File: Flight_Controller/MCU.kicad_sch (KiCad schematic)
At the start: 1 part, among them U1 STM32H743VITx

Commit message: Schem V1 Done!
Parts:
- added C16, C18, C19, C20, C21, C22, C23, C27: 100nF, PCM_JLCPCB:C_0603, symbol PCM_JLCPCB-Capacitors:0603,100nF
- added C17: 4.7uF, PCM_JLCPCB:C_0603, symbol PCM_JLCPCB-Capacitors:0603,4.7uF
- added C25, C26: 12pF, PCM_JLCPCB:C_0603, symbol PCM_JLCPCB-Capacitors:0603,12pF
- added C28, C29: 2.2uF, PCM_JLCPCB:C_0603, symbol PCM_JLCPCB-Capacitors:0603,2.2uF
- added J10: USB_C_Receptacle_USB2.0_16P, symbol Connector:USB_C_Receptacle_USB2.0_16P
- added J11: Conn_ARM_SWD_TagConnect_TC2030-NL, Connector:Tag-Connect_TC2030-IDC-NL_2x03_P1.27mm_Vertical, symbol Connector:Conn_ARM_SWD_TagConnect_TC2030-NL
- added J13: SM06B-GHS-TB, symbol Connector_Generic:Conn_01x06
- added J14: VTX, symbol Connector_Generic:Conn_01x06
- added J6: ESC->FC DSHOT and Telem, symbol Connector:Conn_01x08_Socket
- added J7: ELRS Reciever, symbol Connector:Conn_01x04_Socket
- added J9: Conn_01x03_Socket, symbol Connector:Conn_01x03_Socket
- added R11, R12: 5.1kΩ, PCM_JLCPCB:R_0603, symbol PCM_JLCPCB-Resistors:0603,5.1kΩ
- added R13: 0Ω, PCM_JLCPCB:R_0603, symbol PCM_JLCPCB-Resistors:0603,0Ω
- added R14, R2: 10kΩ, PCM_JLCPCB:R_0603, symbol PCM_JLCPCB-Resistors:0603,10kΩ
- added SW1: SW_SPST, symbol Switch:SW_SPST
- added U7: TPD2EUSB30ADRTR, Flight_Controller:DRT3-L, symbol Flight_Controller:TPD2EUSB30ADRTR
- added XTAL1: 8MHZ-8pF, Flight_Controller:XTAL_NX3225GD-8MHZ-STD-CRA-3_NDK-L, symbol Flight_Controller:NX3225GD-8MHZ-STD-CRA-3
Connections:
- net GND: now reaches U1.10 (VSS), U1.26 (VSS), U1.49 (VSS), U1.74 (VSS), U1.99 (VSS)
- net GND: now also U1.19 (VSSA), C16.2, C17.2, C18.2, C19.2, C20.2, C21.2, C22.2, C23.2, C25.1, C26.1, C27.1, C28.2, C29.2, J10.A1 (GND), J10.A12 (GND), J10.B1 (GND), J10.B12 (GND), J10.SH (SHIELD), J11.5 (GND), J13.6 (Pin_6), J14.6 (Pin_6), J6.7 (Pin_7), J6.8 (Pin_8), J7.4 (Pin_4), J9.3 (Pin_3), R11.1, R12.1, R2.2, U7.3 (GND)
- net +3V3: now reaches U1.100 (VDD)
- net +3V3: now also U1.11 (VDD), U1.20 (VREF+), U1.21 (VDDA), U1.27 (VDD), U1.50 (VDD), U1.6 (VBAT), U1.75 (VDD), C16.1, C17.1, C18.1, C19.1, C20.1, C21.1, C22.1, C23.1, J11.1 (VCC), J13.1 (Pin_1), R13.1, R14.1
- net OSC_IN: now reaches U1.12 (PH0)
- net OSC_IN: now also C25.2, XTAL1.1
- net OSC_OUT: now reaches U1.13 (PH1)
- net OSC_OUT: now also C26.2, XTAL1.2
- net NRST: now reaches U1.14 (NRST)
- net NRST: now also C27.2, J11.3 (~{RESET}), J13.3 (Pin_3), SW1.2 (B)
- net VTX_TX: now reaches U1.22 (PA0)
- net VTX_TX: now also J14.3 (Pin_3)
- net VTX_RX: now reaches U1.23 (PA1)
- net VTX_RX: now also J14.2 (Pin_2)
- net ELRS_TX: now reaches U1.24 (PA2)
- net ELRS_TX: now also J7.3 (Pin_3)
- net ELRS_RX: now reaches U1.25 (PA3)
- net ELRS_RX: now also J7.2 (Pin_2)
- net ADC_CURR: now reaches U1.28 (PA4)
- net ADC_CURR: now also J6.1 (Pin_1)
- net M1_DSHOT: now reaches U1.30 (PA6)
- net M1_DSHOT: now also J6.3 (Pin_3)
- net M2_DSHOT: now reaches U1.31 (PA7)
- net M2_DSHOT: now also J6.4 (Pin_4)
- net M3_DSHOT: now reaches U1.34 (PB0)
- net M3_DSHOT: now also J6.5 (Pin_5)
- net M4_DSHOT: now reaches U1.35 (PB1)
- net M4_DSHOT: now also J6.6 (Pin_6)
- net TELEM_RX: now reaches U1.47 (PB11)
- net TELEM_RX: now also J6.2 (Pin_2)
- net at U1.48 (VCAP): now also C29.1
- net IMU_SPI_CS: now reaches U1.51 (PB12)
- net IMU_SPI_SCK: now reaches U1.52 (PB13)
- net IMU_SPI_SDO: now reaches U1.53 (PB14)
- net IMU_SPI_SDI: now reaches U1.54 (PB15)
- net OSD_LOS: now reaches U1.65 (PC8)
- net OSD_VS: now reaches U1.66 (PC9)
- net D-: now reaches U1.70 (PA11)
- net D-: now also J10.A7 (D-), J10.B7 (D-), U7.2 (D-)
- net D+: now reaches U1.71 (PA12)
- net D+: now also J10.A6 (D+), J10.B6 (D+), U7.1 (D+)
- net SWDIO: now reaches U1.72 (PA13)
- net SWDIO: now also J11.2 (SWDIO), J13.4 (Pin_4)
- net at U1.73 (VCAP): now also C28.1
- net SWCLK: now reaches U1.76 (PA14)
- net SWCLK: now also J11.4 (SWCLK), J13.5 (Pin_5)
- net OSD_SPI_CS: now reaches U1.77 (PA15)
- net SPI_CLK: now reaches U1.78 (PC10)
- net SPI_SDO: now reaches U1.79 (PC11)
- net SPI_SDI: now reaches U1.80 (PC12)
- net IMU_INT: now reaches U1.81 (PD0)
- net LPS_INT: now reaches U1.82 (PD1)
- net LPS_SPI_CS: now reaches U1.83 (PD2)
- net BB_SPI_CS: now reaches U1.84 (PD3)
- net SWO: now reaches U1.89 (PB3)
- net SWO: now also J11.6 (SWO), J13.2 (Pin_2)
- net BOOT0: now reaches U1.94 (BOOT0)
- net BOOT0: now also R13.2, R2.1
- new net: R14.2, SW1.1 (A)
- new net +5V: J14.1 (Pin_1), J7.1 (Pin_1), J9.1 (Pin_1)
- new net +5V_USB: J10.A4 (VBUS), J10.A9 (VBUS), J10.B4 (VBUS), J10.B9 (VBUS)
- new net CC1: J10.A5 (CC1), R11.2
- new net CC2: J10.B5 (CC2), R12.2
- new net VIDEO_IN: J9.2 (Pin_2)
- new net VIDEO_OUT: J14.4 (Pin_4), J14.5 (Pin_5)
- no-connect marks 0 -> 2
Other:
- note added: "COMMUNICATION CONNECTORS"
- note added: "DEBUG CONNECTORS"
- note added: "MCU"
- note added: "USB"
- moved on the sheet: U1

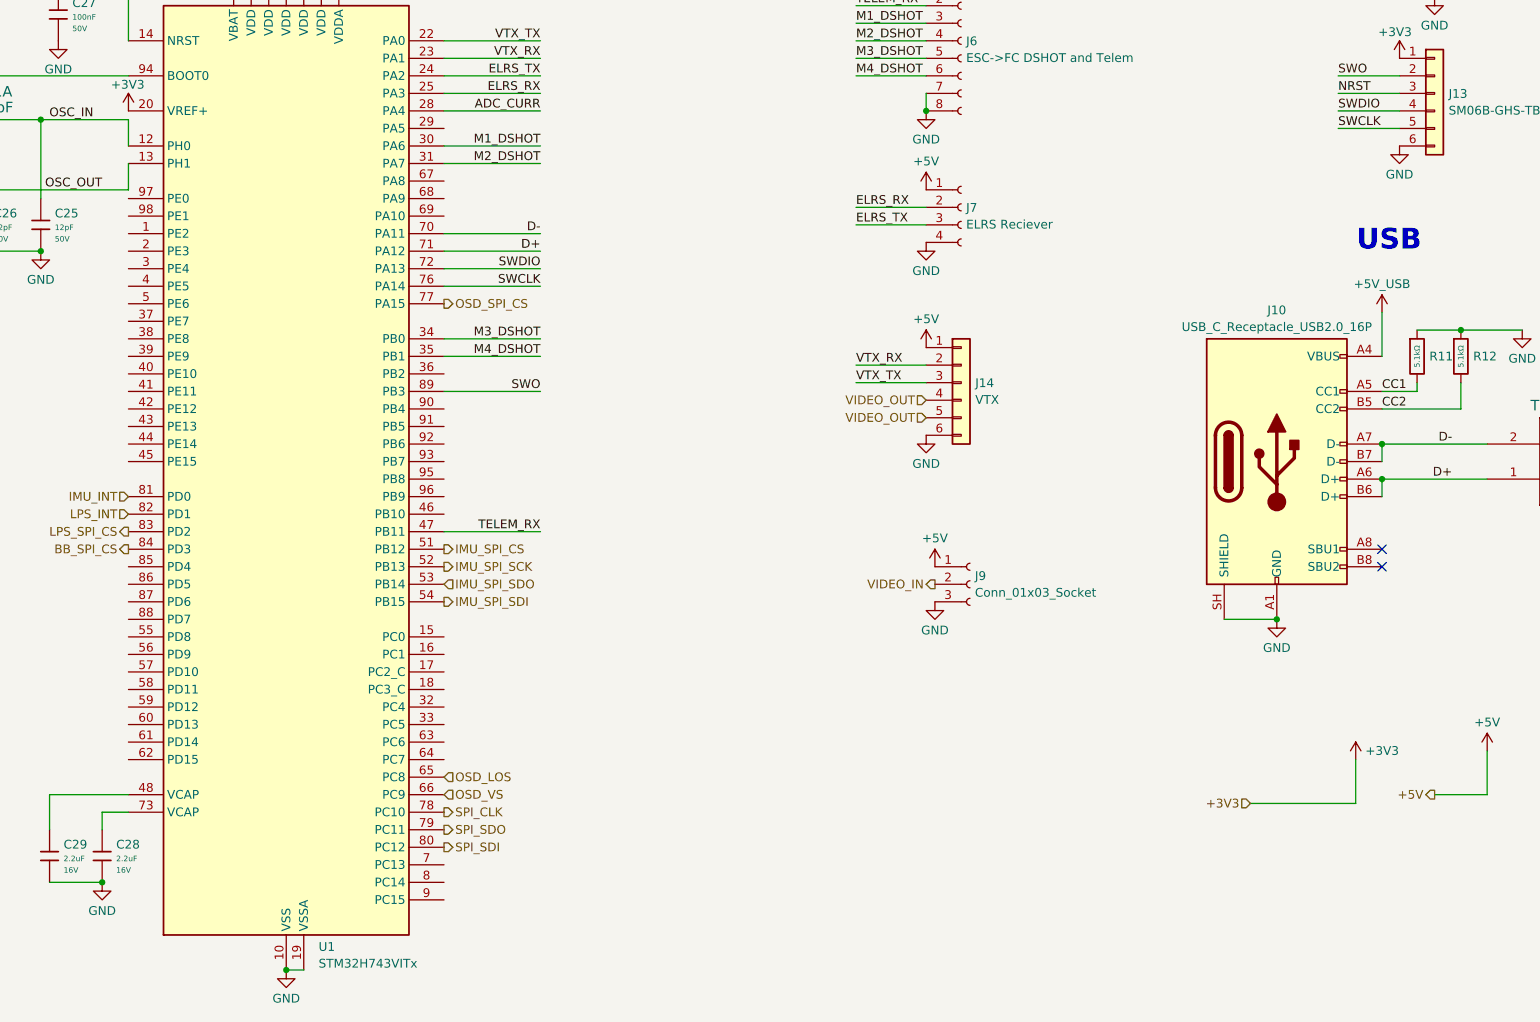
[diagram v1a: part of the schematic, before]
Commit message: Fixed ERC errors
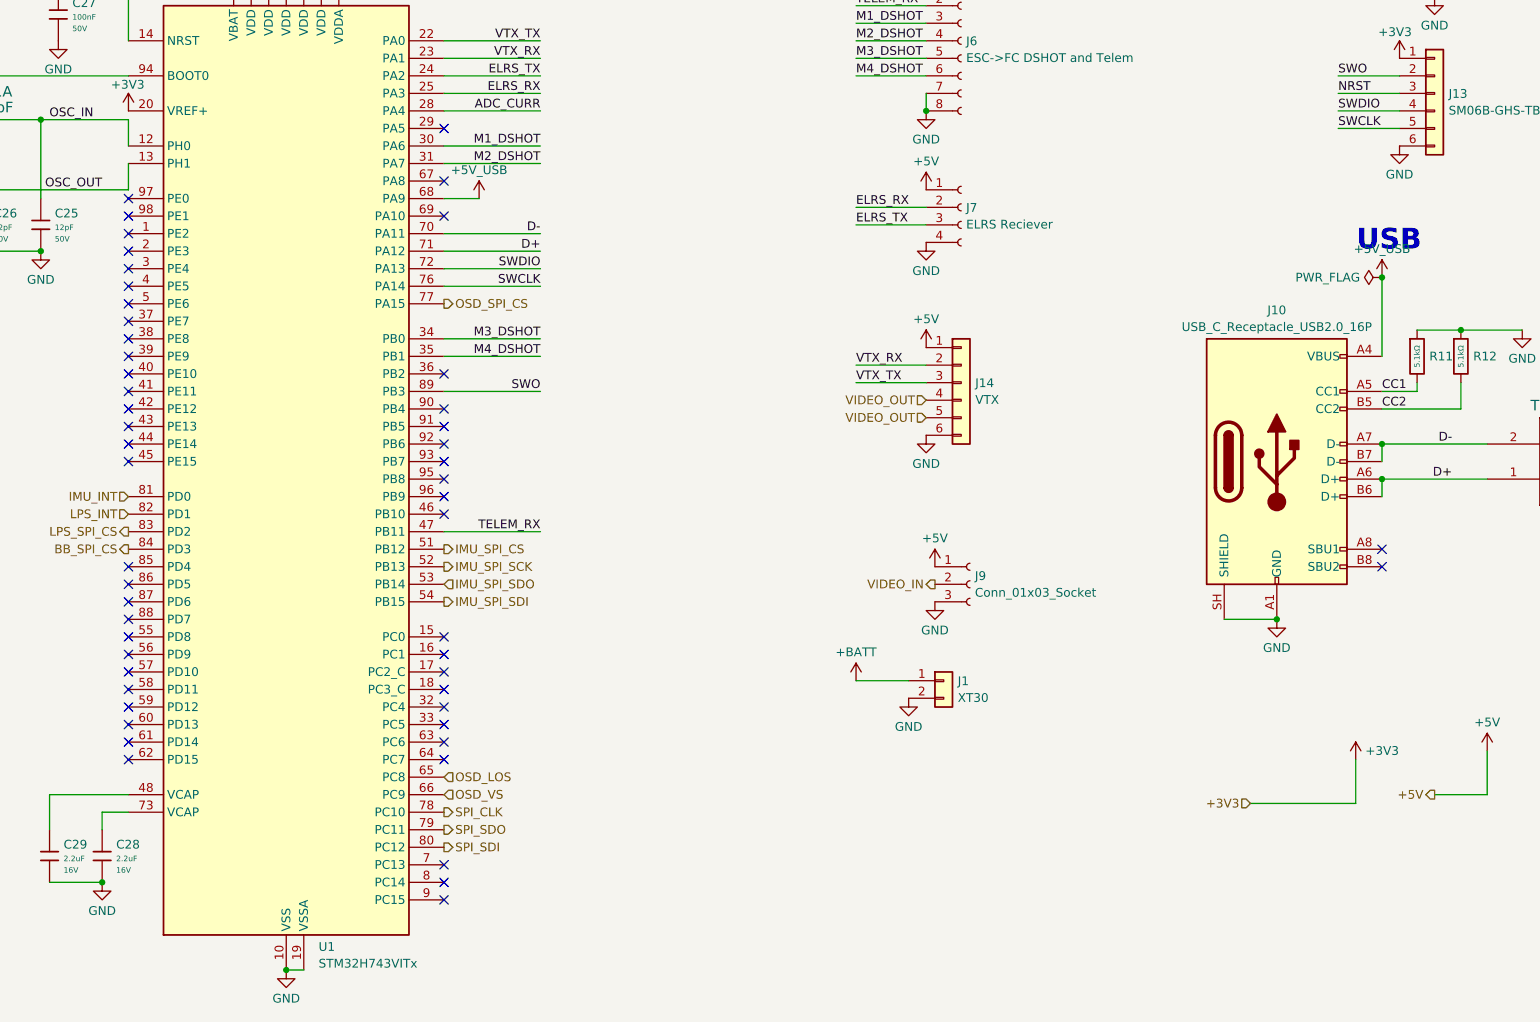
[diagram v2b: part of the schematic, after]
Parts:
- added J1: XT30, symbol Connector_Generic:Conn_01x02
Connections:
- net +5V_USB: now also U1.68 (PA9)
- net +BATT: now also J1.1 (Pin_1)
- net GND: now also J1.2 (Pin_2)
- no-connect marks 2 -> 52

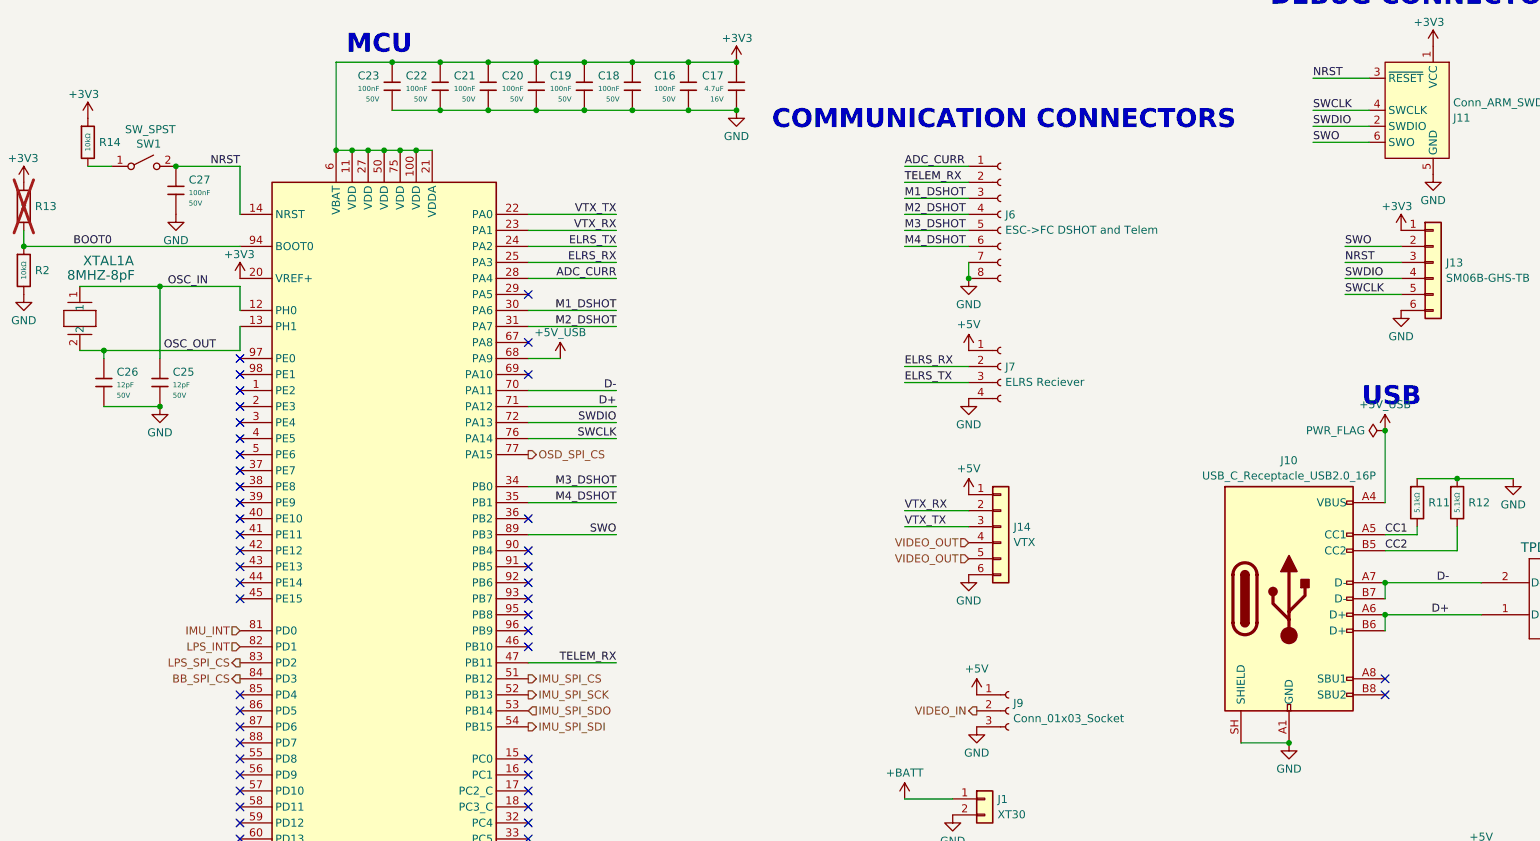
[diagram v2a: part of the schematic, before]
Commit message: Set footprints
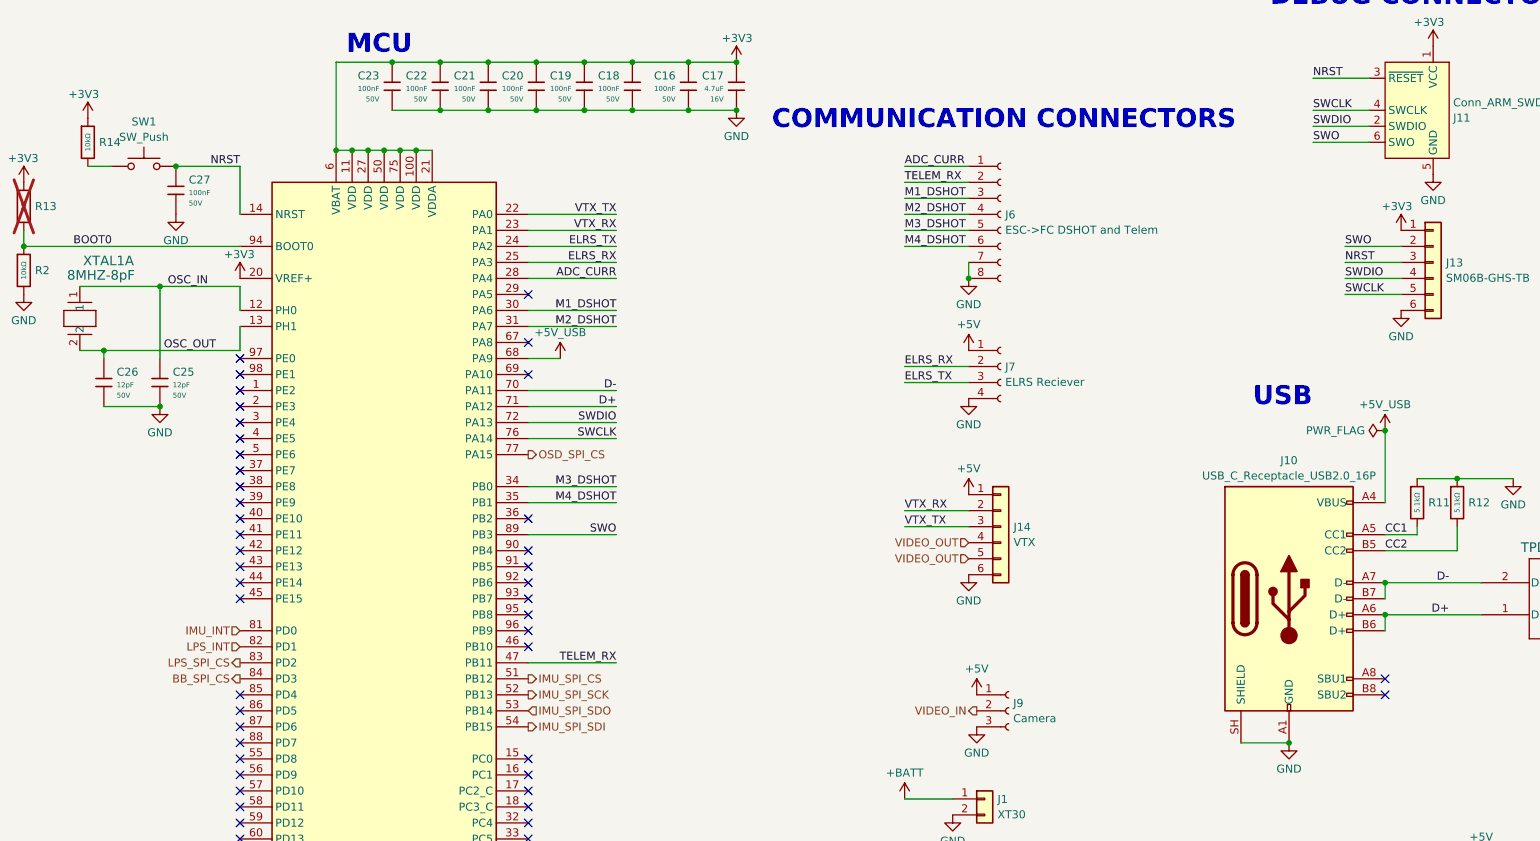
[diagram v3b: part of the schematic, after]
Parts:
- removed SW1: SW_SPST, symbol Switch:SW_SPST
- added SW1: SW_Push, Resistor_SMD:R_0805_2012Metric, symbol Switch:SW_Push
- J1: footprint (none) -> Connector_AMASS:AMASS_XT30PW-M_1x02_P2.50mm_Horizontal
- J10: footprint (none) -> Connector_USB:USB_C_Receptacle_GCT_USB4110
- J13, J14: footprint (none) -> Connector_JST:JST_GH_SM06B-GHS-TB_1x06-1MP_P1.25mm_Horizontal
- J6: footprint (none) -> Connector_JST:JST_GH_SM08B-GHS-TB_1x08-1MP_P1.25mm_Horizontal
- J7: footprint (none) -> Connector_JST:JST_GH_SM03B-GHS-TB_1x03-1MP_P1.25mm_Horizontal
- J9: value Conn_01x03_Socket -> Camera; footprint (none) -> Connector_JST:JST_GH_SM02B-GHS-TB_1x02-1MP_P1.25mm_Horizontal
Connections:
- net NRST: now also SW1.2
- net at R14.2: now also SW1.1

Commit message: Added labels in schem
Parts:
- removed J1: XT30, Connector_AMASS:AMASS_XT30PW-M_1x02_P2.50mm_Horizontal, symbol Connector_Generic:Conn_01x02
- J7: footprint Connector_JST:JST_GH_SM03B-GHS-TB_1x03-1MP_P1.25mm_Horizontal -> Connector_JST:JST_GH_SM04B-GHS-TB_1x04-1MP_P1.25mm_Horizontal
- J9: footprint Connector_JST:JST_GH_SM02B-GHS-TB_1x02-1MP_P1.25mm_Horizontal -> Connector_JST:JST_GH_SM03B-GHS-TB_1x03-1MP_P1.25mm_Horizontal
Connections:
- net +BATT: now also J6.7 (Pin_7)
- net GND: no longer J6.7 (Pin_7)
- net OSD_SPI_CS: now also U1.85 (PD4); no longer U1.77 (PA15)
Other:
- note added: "DNP resistor can be shorted to allow for DFU mode. VBATT and vdda tied to 3v3."
- note added: "TVS reverse stand-off 5v5,clamp 8v cc tied pulled down 5.1k to recognize as sink"
- moved on the sheet: C16, C17, C18, C19, C20, C21, C22, C23, C25, C26, C27, C28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
